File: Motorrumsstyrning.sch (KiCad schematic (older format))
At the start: 49 parts, among them J1 SD_Card_Connector, J10 Jumper, J11 Jumper, J12 Jumper, J13 Conn_01x09, J14 Screw_Terminal_01x10, J15 Screw_Terminal_01x10, J2 Jumper, J3 Jumper, J4 Jumper, J5 Jumper, J6 Jumper, J7 Jumper, J8 Jumper, J9 Jumper, Q1 BC337, Q2 BC337, U1 NUCLEO-F303K8, U2 LM1084-5.0, U3 MCP2551-I-P

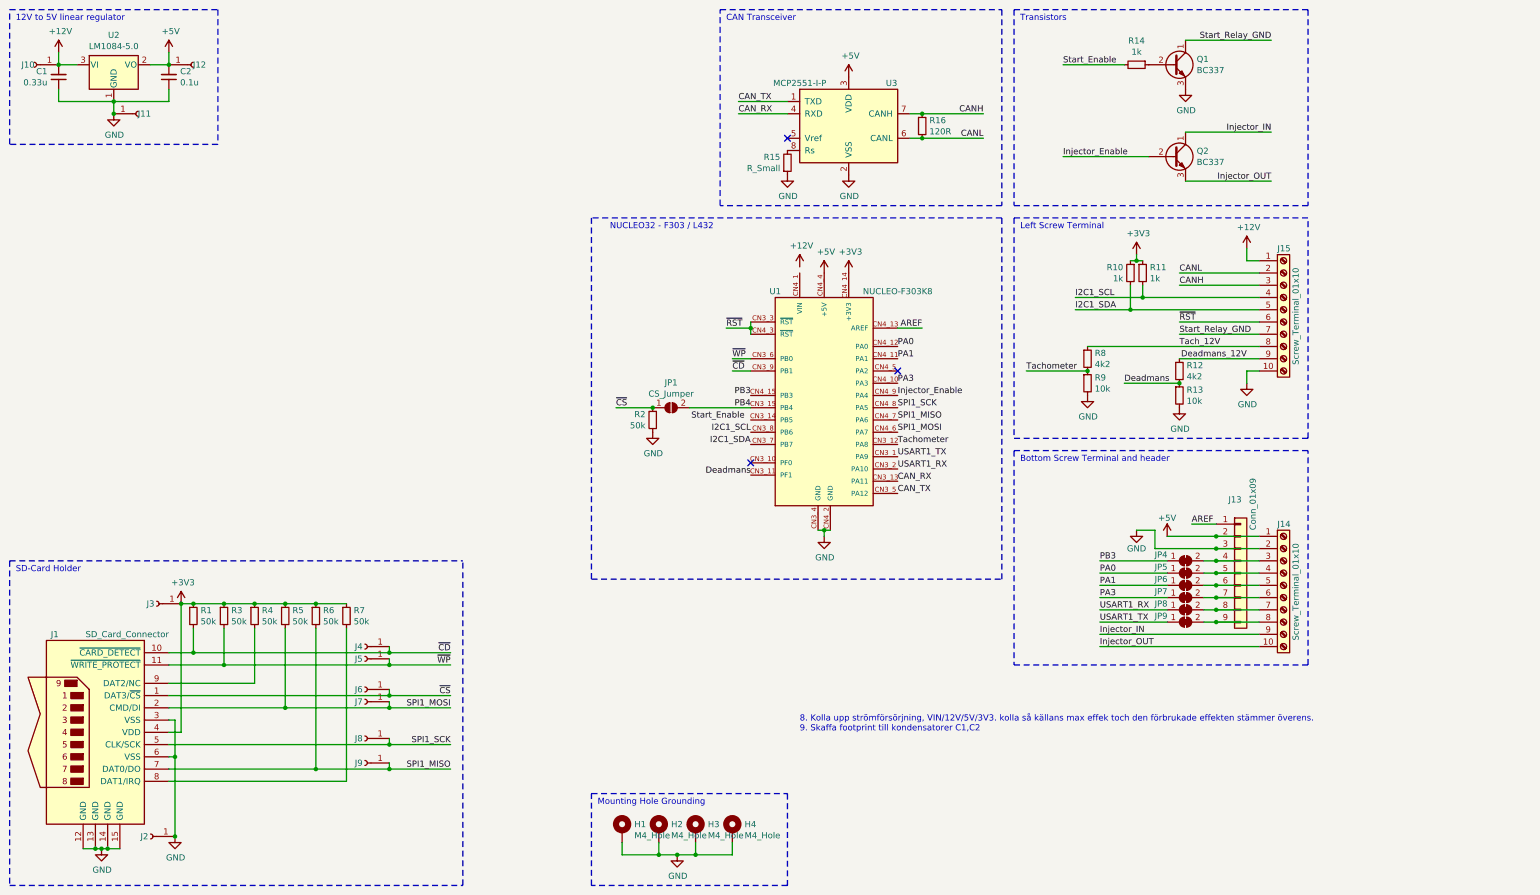
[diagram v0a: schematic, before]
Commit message: Fixed Silkscreen
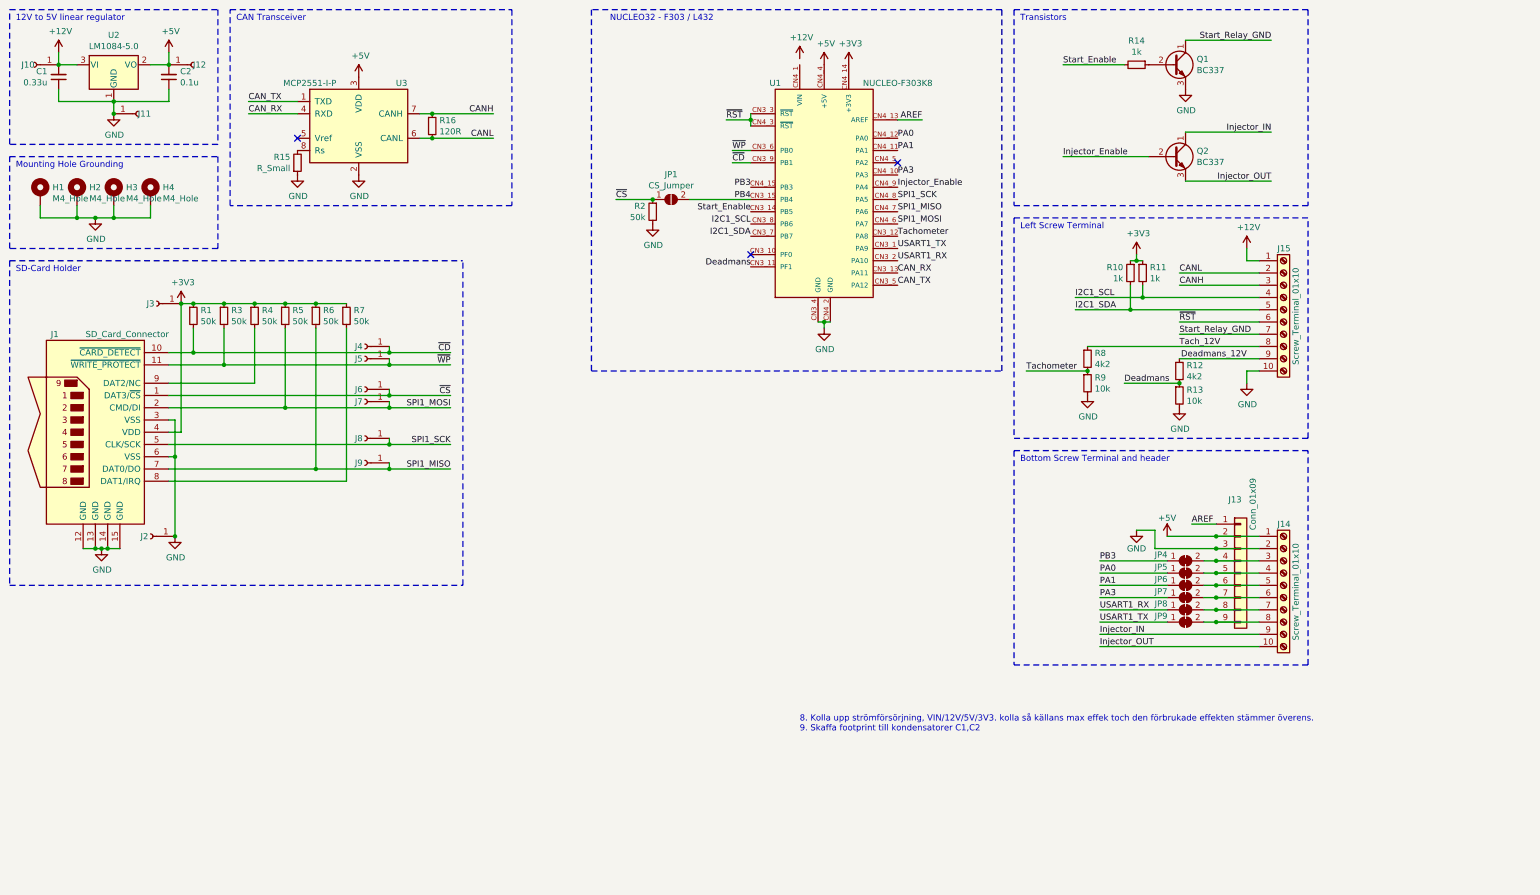
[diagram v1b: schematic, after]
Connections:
- net Start_Enable: now also U1.CN3_14 (PB5)
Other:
- moved on the sheet: H1, H2, H3, H4, J1, J2, J3, J4, J5, J6, J7, J8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

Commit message: Finalization and Gerber generation
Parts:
- C1, C2: footprint (none) -> Capacitor_SMD:C_1206_3216Metric_Pad1.42x1.75mm_HandSolder
- renumbered J10 to J1, J8 to J10, J9 to J11, J1 to J12, J2 to J13, J13 to J14, J14 to J15, J12 to J2, J11 to J3, J3 to J4, J15 to J5, J4 to J6, J5 to J7, J6 to J8, J7 to J9, JP4 to JP2, JP5 to JP3, JP6 to JP4, JP7 to JP5, JP8 to JP6, JP9 to JP7, R14 to R1, R5 to R10, R6 to R11, R7 to R12, R8 to R13, R9 to R14, R12 to R15, R13 to R16, R16 to R2, R15 to R3, R2 to R4, R10 to R5, R11 to R6, R1 to R7, R3 to R8, R4 to R9, U2 to U1, U3 to U2, U1 to U3
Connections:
- net +3V3: now also J14.1 (Pin_1)
- net AREF: no longer J14.1 (Pin_1)
- no-connect marks 3 -> 4
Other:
- note removed: "8. Kolla upp strömförsörjning, VIN/12V/5V/3V3. kolla så källans max effek toch den förbrukade effekten stämmer överens.\n9. Skaffa footprint till kondensatorer C1,C2"

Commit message: Update
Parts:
- added JP8: Injector_Override, Jumper:SolderJumper-2_P1.3mm_Open_TrianglePad1.0x1.5mm, symbol Jumper:SolderJumper_2_Open
- added JP9: Start_Relay_Override, Jumper:SolderJumper-2_P1.3mm_Open_TrianglePad1.0x1.5mm, symbol Jumper:SolderJumper_2_Open
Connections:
- net GND: now also JP9.1 (A)
- net Injector_IN: now also JP8.2 (B)
- net Injector_OUT: now also JP8.1 (A)
- net Start_Relay_GND: now also JP9.2 (B)
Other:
- moved on the sheet: Q1, Q2, R1
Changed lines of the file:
@@
 L Transistor_BJT:BC337 Q1
 U 1 1 60C819FD
-P 10050 1000
-F 0 "Q1" H 10241 1046 50  0000 L CNN
-F 1 "BC337" H 10241 955 50  0000 L CNN
-F 2 "Package_TO_SOT_THT:TO-92_Inline" H 10250 925 50  0001 L CIN
-F 3 "https://diotec.com/tl_files/diotec/files/pdf/datasheets/bc337.pdf" H 10050 1000 50  0001 L CNN
-	1    10050 1000
-	1    0    0    -1
-$EndComp
-Text Label 10850 800  2    50   ~ 0
+P 9800 1000
+F 0 "Q1" H 9991 1046 50  0000 L CNN
+F 1 "BC337" H 9991 955 50  0000 L CNN
+F 2 "Package_TO_SOT_THT:TO-92_Inline" H 10000 925 50  0001 L CIN
+F 3 "https://diotec.com/tl_files/diotec/files/pdf/datasheets/bc337.pdf" H 9800 1000 50  0001 L CNN
+	1    9800 1000
+	1    0    0    -1
+$EndComp
+Text Label 11100 800  2    50   ~ 0
 Start_Relay_GND
 $Comp
 L power:GND #PWR06
 U 1 1 60C82964
-P 10150 1200
-F 0 "#PWR06" H 10150 950 50  0001 C CNN
-F 1 "GND" H 10155 1027 50  0000 C CNN
-F 2 "" H 10150 1200 50  0001 C CNN
-F 3 "" H 10150 1200 50  0001 C CNN
-	1    10150 1200
+P 9900 1200
+F 0 "#PWR06" H 9900 950 50  0001 C CNN
+F 1 "GND" H 9905 1027 50  0000 C CNN
+F 2 "" H 9900 1200 50  0001 C CNN
+F 3 "" H 9900 1200 50  0001 C CNN
+	1    9900 1200
 	1    0    0    -1
 $EndComp
@@
 L Device:R_Small R1
 U 1 1 60C832BB
-P 9750 1000
-F 0 "R1" V 9554 1000 50  0000 C CNN
-F 1 "1k" V 9645 1000 50  0000 C CNN
-F 2 "Resistor_THT:R_Axial_DIN0207_L6.3mm_D2.5mm_P7.62mm_Horizontal" H 9750 1000 50  0001 C CNN
-F 3 "~" H 9750 1000 50  0001 C CNN
-	1    9750 1000
+P 9500 1000
+F 0 "R1" V 9304 1000 50  0000 C CNN
+F 1 "1k" V 9395 1000 50  0000 C CNN
+F 2 "Resistor_THT:R_Axial_DIN0207_L6.3mm_D2.5mm_P7.62mm_Horizontal" H 9500 1000 50  0001 C CNN
+F 3 "~" H 9500 1000 50  0001 C CNN
+	1    9500 1000
 	0    1    1    0
 $EndComp
-Text Label 9150 1000 0    50   ~ 0
+Text Label 8900 1000 0    50   ~ 0
 Start_Enable
 Wire Wire Line
-	9650 1000 9150 1000
+	9400 1000 8900 1000
 Text Label 10850 1550 2    50   ~ 0
 Injector_IN
@@
 L Transistor_BJT:BC337 Q2
 U 1 1 60C8DD08
-P 10050 1750
-F 0 "Q2" H 10241 1796 50  0000 L CNN
-F 1 "BC337" H 10241 1705 50  0000 L CNN
-F 2 "Package_TO_SOT_THT:TO-92_Inline" H 10250 1675 50  0001 L CIN
-F 3 "https://diotec.com/tl_files/diotec/files/pdf/datasheets/bc337.pdf" H 10050 1750 50  0001 L CNN
-	1    10050 1750
+P 9650 1750
+F 0 "Q2" H 9841 1796 50  0000 L CNN
+F 1 "BC337" H 9841 1705 50  0000 L CNN
+F 2 "Package_TO_SOT_THT:TO-92_Inline" H 9850 1675 50  0001 L CIN
+F 3 "https://diotec.com/tl_files/diotec/files/pdf/datasheets/bc337.pdf" H 9650 1750 50  0001 L CNN
+	1    9650 1750
 	1    0    0    -1
 $EndComp
@@
 	10850 1950 10150 1950
 Wire Wire Line
-	10150 1550 10850 1550
+	9750 1550 10150 1550
 Text Label 7800 2000 0    50   ~ 0
 Injector_Enable
-Text Label 9150 1750 0    50   ~ 0
+Text Label 8900 1750 0    50   ~ 0
 Injector_Enable
 Wire Wire Line
-	9150 1750 9850 1750
+	8900 1750 9450 1750
 Text Label 7800 1900 0    50   ~ 0
 PA3
@@
 Text Notes 8800 2350 0    50   ~ 0
 Left Screw Terminal
-Wire Wire Line
-	10150 800  10850 800
 Wire Notes Line
 	11150 2150 8750 2150
@@
 	1    0    0    -1
 $EndComp
+$Comp
+L Jumper:SolderJumper_2_Open JP9
+U 1 1 613A7272
+P 10300 1000
+F 0 "JP9" V 10250 1100 50  0000 L CNN
+F 1 "Start_Relay_Override" V 10350 1100 50  0000 L CNN
+F 2 "Jumper:SolderJumper-2_P1.3mm_Open_TrianglePad1.0x1.5mm" H 10300 1000 50  0001 C CNN
+F 3 "~" H 10300 1000 50  0001 C CNN
+	1    10300 1000
+	0    1    -1   0
+$EndComp
+$Comp
+L Jumper:SolderJumper_2_Open JP8
+U 1 1 613B8773
+P 10150 1750
+F 0 "JP8" V 10100 1850 50  0000 L CNN
+F 1 "Injector_Override" V 10200 1850 50  0000 L CNN
+F 2 "Jumper:SolderJumper-2_P1.3mm_Open_TrianglePad1.0x1.5mm" H 10150 1750 50  0001 C CNN
+F 3 "~" H 10150 1750 50  0001 C CNN
+	1    10150 1750
+	0    1    -1   0
+$EndComp
+Wire Wire Line
+	10150 1600 10150 1550
+Connection ~ 10150 1550
+Wire Wire Line
+	10150 1550 10850 1550
+Wire Wire Line
+	10150 1900 10150 1950
+Connection ~ 10150 1950
+Wire Wire Line
+	10150 1950 9750 1950
+Wire Wire Line
+	9900 800  10300 800
+Wire Wire Line
+	10300 850  10300 800
+Connection ~ 10300 800
+Wire Wire Line
+	10300 800  11100 800
+Wire Wire Line
+	10300 1150 10300 1200
+Wire Wire Line
+	10300 1200 9900 1200
+Connection ~ 9900 1200
 $EndSCHEMATC
